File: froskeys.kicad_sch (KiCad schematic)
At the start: 25 parts, among them SW1 MX, SW10 RotaryEncoder_Switch, SW2 MX, SW3 MX, SW4 MX, SW5 MX, SW6 MX, SW7 MX, SW8 MX, SW9 MX, U1 XIAO-RP2040-DIP, U2 OLED

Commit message: Optimise
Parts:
- removed U2: OLED, OLED:SSD1306-0.91-OLED-4pin-128x32, symbol OLED:0.91{dblquote}_128x32_I2C_OLED_Display
- added J1: OLED, OLED:SSD1306-0.91-OLED-4pin-128x32, symbol Connector:Conn_01x04_Pin
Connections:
- net +5V: now also J1.2 (Pin_2)
- net GND: now also J1.1 (Pin_1)
- net SCL: now also J1.3 (Pin_3)
- net SDA: now also J1.4 (Pin_4)
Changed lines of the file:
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@@
 	(global_label "SDA"
 		(shape input)
-		(at 208.28 118.11 180)
+		(at 208.28 118.11 0)
 		(fields_autoplaced yes)
 		(effects
@@
 				(size 1.27 1.27)
 			)
-			(justify right)
+			(justify left)
 		)
 		(property "Intersheetrefs" "${INTERSHEET_REFS}"
-			(at 201.7267 118.11 0)
-			(effects
-				(font
-					(size 1.27 1.27)
-				)
-				(justify right)
+			(at 214.8333 118.11 0)
+			(effects
+				(font
+					(size 1.27 1.27)
+				)
+				(justify left)
 				(hide yes)
 			)
@@
 	(global_label "SCL"
 		(shape input)
-		(at 208.28 115.57 180)
+		(at 208.28 115.57 0)
 		(fields_autoplaced yes)
 		(effects
@@
 				(size 1.27 1.27)
 			)
-			(justify right)
+			(justify left)
 		)
 		(property "Intersheetrefs" "${INTERSHEET_REFS}"
-			(at 201.7872 115.57 0)
-			(effects
-				(font
-					(size 1.27 1.27)
-				)
-				(justify right)
+			(at 214.7728 115.57 0)
+			(effects
+				(font
+					(size 1.27 1.27)
+				)
+				(justify left)
 				(hide yes)
 			)
@@
 	(symbol
 		(lib_id "power:GND")
-		(at 208.28 110.49 270)
+		(at 208.28 110.49 90)
 		(unit 1)
 		(exclude_from_sim no)
@@
 		(fields_autoplaced yes)
 		(property "Reference" "#PWR03"
-			(at 201.93 110.49 0)
+			(at 214.63 110.49 0)
 			(effects
 				(font
@@
 		)
 		(property "Value" "GND"
-			(at 204.47 110.4899 90)
+			(at 212.09 110.4899 90)
 			(effects
 				(font
@@
 	)
 	(symbol
+		(lib_id "Connector:Conn_01x04_Pin")
+		(at 203.2 113.03 0)
+		(unit 1)
+		(exclude_from_sim no)
+		(in_bom yes)
+		(on_board yes)
+		(dnp no)
+		(fields_autoplaced yes)
+		(property "Reference" "J1"
+			(at 203.835 105.41 0)
+			(effects
+				(font
+					(size 1.27 1.27)
+				)
+			)
+		)
+		(property "Value" "OLED"
+			(at 203.835 107.95 0)
+			(effects
+				(font
+					(size 1.27 1.27)
+				)
+			)
+		)
+		(property "Footprint" "OLED:SSD1306-0.91-OLED-4pin-128x32"
+			(at 203.2 113.03 0)
+			(effects
+				(font
+					(size 1.27 1.27)
+				)
+				(hide yes)
+			)
+		)
+		(property "Datasheet" "~"
+			(at 203.2 113.03 0)
+			(effects
+				(font
+					(size 1.27 1.27)
+				)
+				(hide yes)
+			)
+		)
+		(property "Description" "Generic connector, single row, 01x04, script generated"
+			(at 203.2 113.03 0)
+			(effects
+				(font
+					(size 1.27 1.27)
+				)
+				(hide yes)
+			)
+		)
+		(pin "2"
+		)
+		(pin "1"
+		)
+		(pin "3"
+		)
+		(pin "4"
+		)
+		(instances
+			(project ""
+				(path "/7f4b6218-3a01-4dd6-a14f-3aa125e7c41a"
+					(reference "J1")
+					(unit 1)
+				)
+			)
+		)
+	)
+	(symbol
 		(lib_id "Diode:1N4148")
 		(at 227.33 71.12 0)
@@
 	(symbol
 		(lib_id "power:+5V")
-		(at 208.28 113.03 90)
+		(at 208.28 113.03 270)
 		(unit 1)
 		(exclude_from_sim no)
@@
 		(fields_autoplaced yes)
 		(property "Reference" "#PWR04"
-			(at 212.09 113.03 0)
+			(at 204.47 113.03 0)
 			(effects
 				(font
@@
 		)
 		(property "Value" "+5V"
-			(at 204.47 113.0299 90)
+			(at 212.09 113.0299 90)
 			(effects
 				(font
@@
 					(unit 1)
 				)
-			)
-		)
-	)
-	(symbol
-		(lib_id "OLED:0.91{dblquote}_128x32_I2C_OLED_Display")
-		(at 215.9 114.3 0)
-		(unit 1)
-		(exclude_from_sim no)
-		(in_bom yes)
-		(on_board yes)
-		(dnp no)
-		(fields_autoplaced yes)
-		(property "Reference" "U2"
-			(at 222.25 113.6649 0)
-			(effects
-				(font
-					(size 1.27 1.27)
-				)
-				(justify left)
-			)
-		)
-		(property "Value" "OLED"
-			(at 222.25 115.57 0)
-			(effects
-				(font
-					(size 1.27 1.27)
-				)
-				(justify left)
-			)
-		)
-		(property "Footprint" "OLED:SSD1306-0.91-OLED-4pin-128x32"
-			(at 215.9 114.3 0)
-			(effects
-				(font
-					(size 1.27 1.27)
-				)
-				(hide yes)
-			)
-		)
-		(property "Datasheet" ""
-			(at 215.9 114.3 0)
-			(effects
-				(font
-					(size 1.27 1.27)
-				)
-				(hide yes)
-			)
-		)
-		(property "Description" ""
-			(at 215.9 114.3 0)
-			(effects
-				(font
-					(size 1.27 1.27)
-				)
-				(hide yes)
-			)
-		)
-		(pin "3"
-		)
-		(pin "4"
-		)
-		(pin "2"
-		)
-		(pin "1"
-		)
-		(instances
-			(project ""
-				(path "/7f4b6218-3a01-4dd6-a14f-3aa125e7c41a"
-					(reference "U2")
-					(unit 1)
-				)

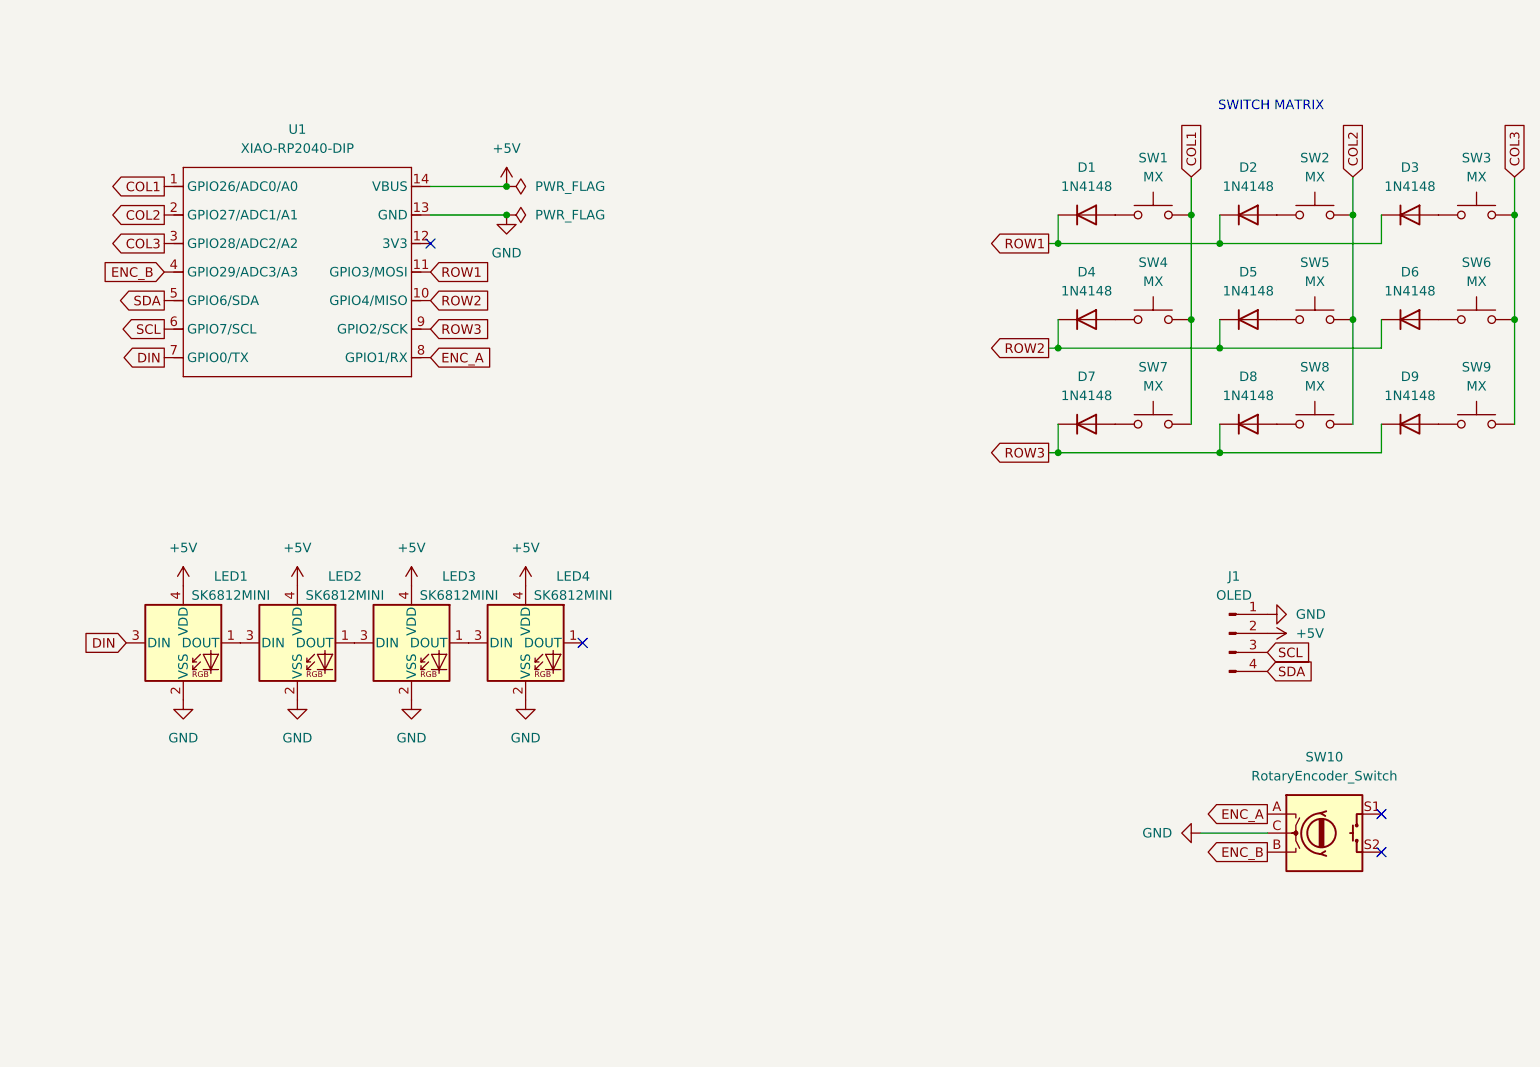
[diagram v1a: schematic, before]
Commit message: Switch to SK6812MINI-E backlighting
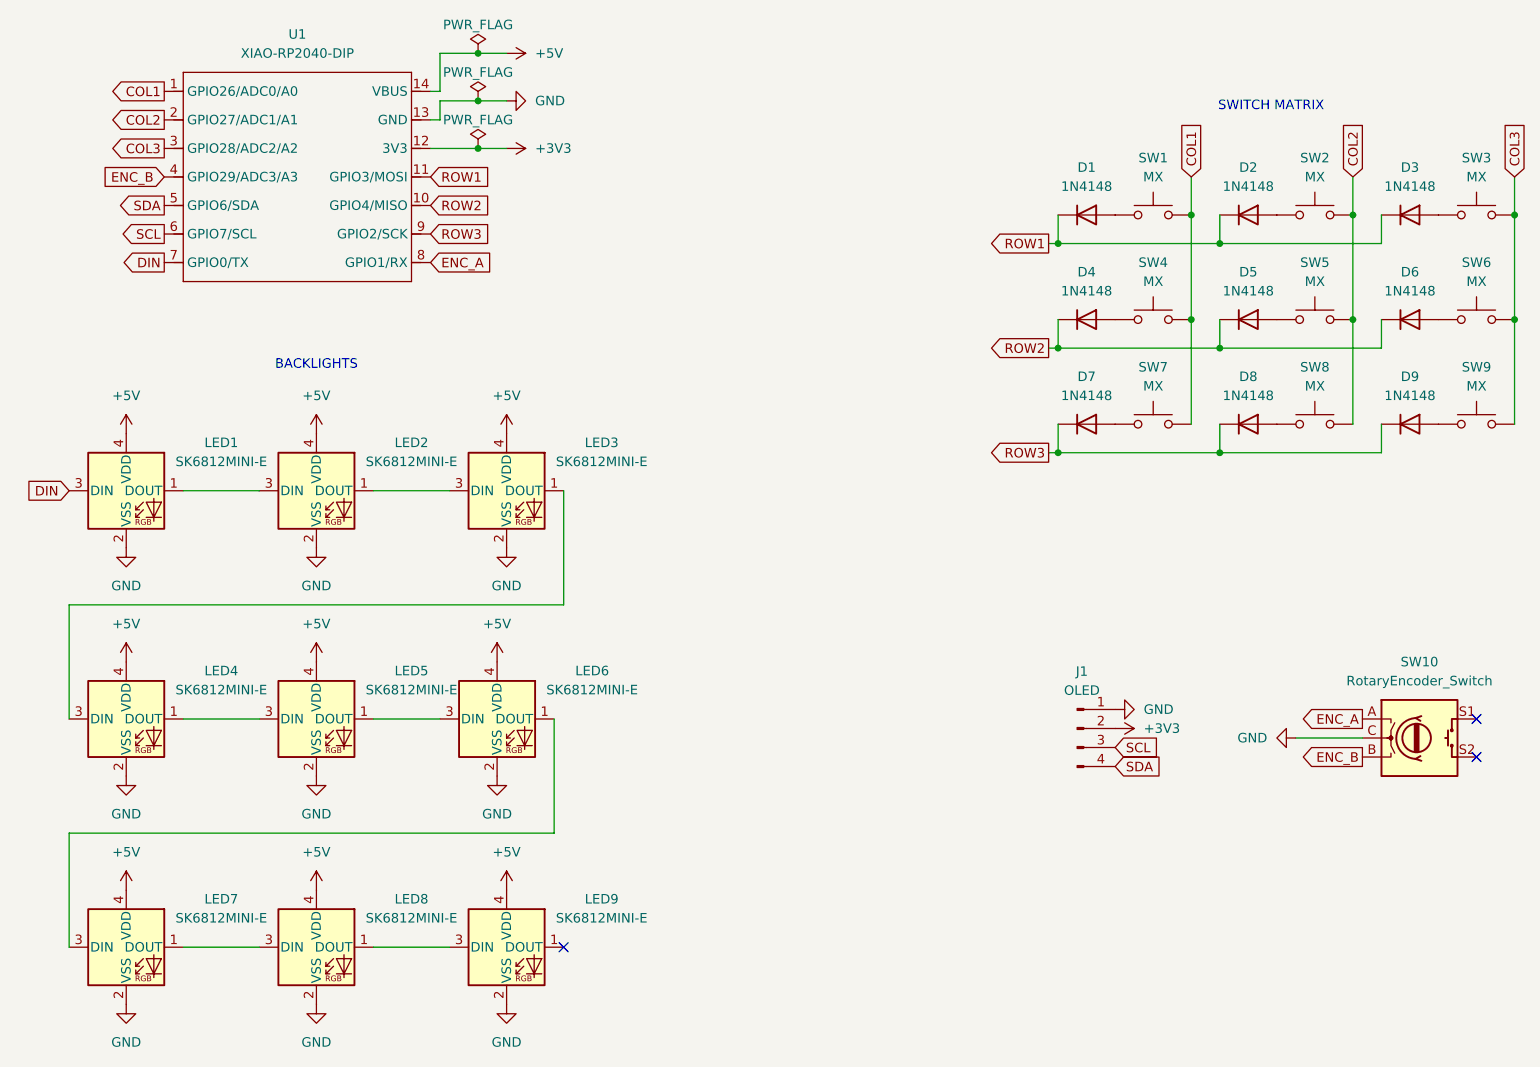
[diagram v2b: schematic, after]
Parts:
- added LED5, LED6, LED7, LED8, LED9: SK6812MINI-E, Keyboard Parts:MX_SK6812MINI-E, symbol LED:SK6812MINI
- LED1, LED2, LED3, LED4: value SK6812MINI -> SK6812MINI-E; footprint LED_SMD:LED_SK6812MINI_PLCC4_3.5x3.5mm_P1.75mm -> Keyboard Parts:MX_SK6812MINI-E
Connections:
- net +5V: now also LED5.4 (VDD), LED6.4 (VDD), LED7.4 (VDD), LED8.4 (VDD), LED9.4 (VDD); no longer J1.2 (Pin_2)
- net GND: now also LED5.2 (VSS), LED6.2 (VSS), LED7.2 (VSS), LED8.2 (VSS), LED9.2 (VSS)
- net at LED4.1 (DOUT): now also LED5.3 (DIN)
- net +3V3: now reaches U1.12 (3V3)
- net +3V3: now also J1.2 (Pin_2)
- new net: LED6.1 (DOUT), LED7.3 (DIN)
- new net: LED5.1 (DOUT), LED6.3 (DIN)
- new net: LED7.1 (DOUT), LED8.3 (DIN)
- new net: LED8.1 (DOUT), LED9.3 (DIN)
- no-connect marks 4 -> 3
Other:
- note added: "BACKLIGHTS"
- moved on the sheet: J1, SW10, U1
